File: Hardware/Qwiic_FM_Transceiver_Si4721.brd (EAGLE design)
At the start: 54.6 x 34.3 mm, 60 parts, among them J1 AUDIO_JACK_3.5MM_SMD, J2 AUDIO_JACK_3.5MM_SMD, J4 QWIIC_RIGHT_ANGLE, J5 QWIIC_RIGHT_ANGLE, U1 SI4721, U3 TPA6111A2DR, Y1 32.768kHz

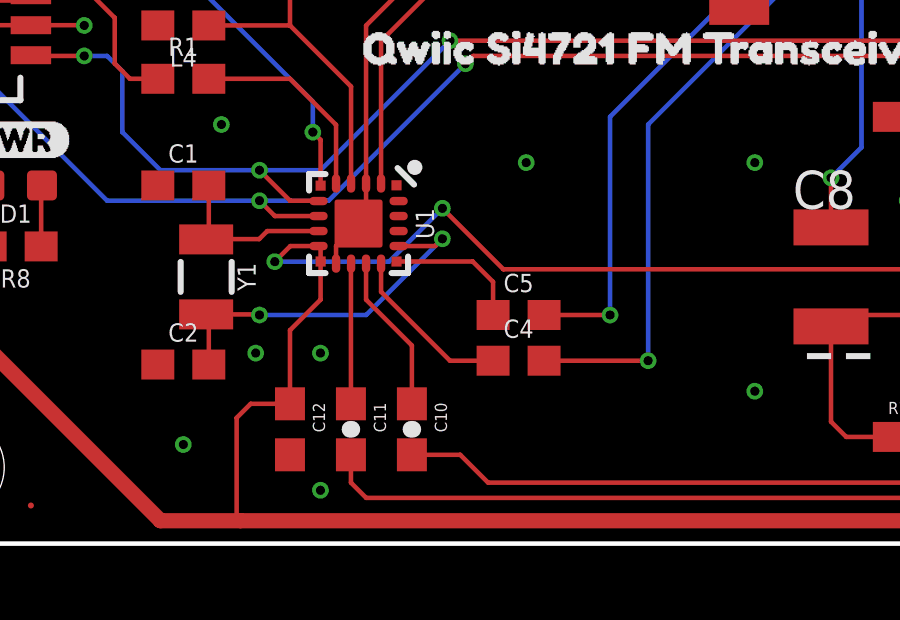
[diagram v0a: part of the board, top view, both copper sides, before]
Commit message: x01 protos ordered
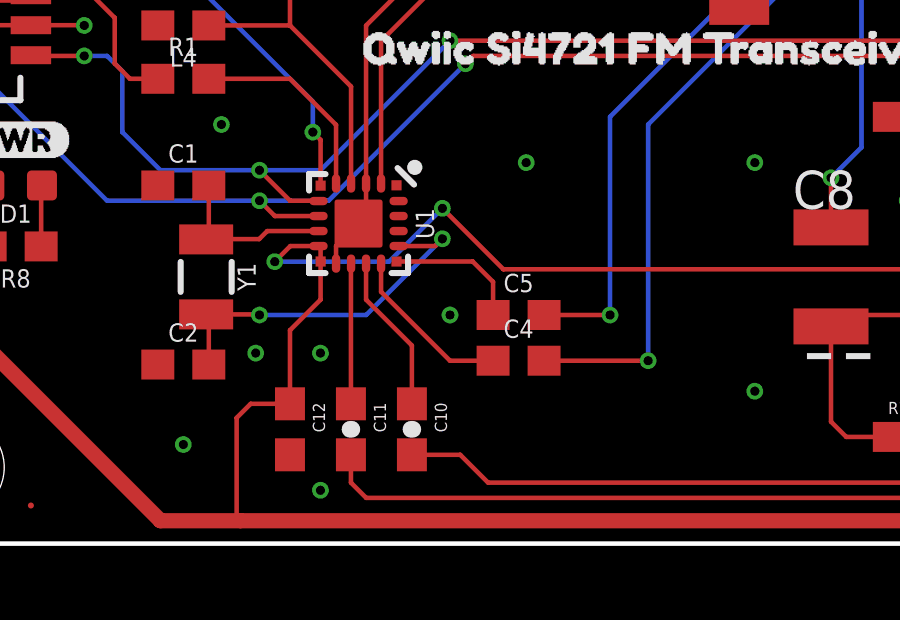
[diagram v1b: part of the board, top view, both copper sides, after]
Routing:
- net GND: vias 17 -> 18
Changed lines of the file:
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@@
 <layer number="23" name="tOrigins" color="15" fill="1" visible="yes" active="yes"/>
 <layer number="24" name="bOrigins" color="15" fill="1" visible="yes" active="yes"/>
-<layer number="25" name="tNames" color="7" fill="1" visible="no" active="yes"/>
-<layer number="26" name="bNames" color="7" fill="1" visible="no" active="yes"/>
-<layer number="27" name="tValues" color="7" fill="1" visible="no" active="yes"/>
-<layer number="28" name="bValues" color="7" fill="1" visible="no" active="yes"/>
-<layer number="29" name="tStop" color="7" fill="3" visible="no" active="yes"/>
-<layer number="30" name="bStop" color="7" fill="6" visible="no" active="yes"/>
-<layer number="31" name="tCream" color="7" fill="4" visible="no" active="yes"/>
-<layer number="32" name="bCream" color="7" fill="5" visible="no" active="yes"/>
-<layer number="33" name="tFinish" color="6" fill="3" visible="no" active="yes"/>
-<layer number="34" name="bFinish" color="6" fill="6" visible="no" active="yes"/>
-<layer number="35" name="tGlue" color="7" fill="4" visible="no" active="yes"/>
-<layer number="36" name="bGlue" color="7" fill="5" visible="no" active="yes"/>
-<layer number="37" name="tTest" color="7" fill="1" visible="no" active="yes"/>
-<layer number="38" name="bTest" color="7" fill="1" visible="no" active="yes"/>
-<layer number="39" name="tKeepout" color="4" fill="11" visible="no" active="yes"/>
-<layer number="40" name="bKeepout" color="1" fill="11" visible="no" active="yes"/>
-<layer number="41" name="tRestrict" color="4" fill="10" visible="no" active="yes"/>
-<layer number="42" name="bRestrict" color="1" fill="10" visible="no" active="yes"/>
-<layer number="43" name="vRestrict" color="2" fill="10" visible="no" active="yes"/>
-<layer number="44" name="Drills" color="7" fill="1" visible="no" active="yes"/>
+<layer number="25" name="tNames" color="7" fill="1" visible="yes" active="yes"/>
+<layer number="26" name="bNames" color="7" fill="1" visible="yes" active="yes"/>
+<layer number="27" name="tValues" color="7" fill="1" visible="yes" active="yes"/>
+<layer number="28" name="bValues" color="7" fill="1" visible="yes" active="yes"/>
+<layer number="29" name="tStop" color="7" fill="3" visible="yes" active="yes"/>
+<layer number="30" name="bStop" color="7" fill="6" visible="yes" active="yes"/>
+<layer number="31" name="tCream" color="7" fill="4" visible="yes" active="yes"/>
+<layer number="32" name="bCream" color="7" fill="5" visible="yes" active="yes"/>
+<layer number="33" name="tFinish" color="6" fill="3" visible="yes" active="yes"/>
+<layer number="34" name="bFinish" color="6" fill="6" visible="yes" active="yes"/>
+<layer number="35" name="tGlue" color="7" fill="4" visible="yes" active="yes"/>
+<layer number="36" name="bGlue" color="7" fill="5" visible="yes" active="yes"/>
+<layer number="37" name="tTest" color="7" fill="1" visible="yes" active="yes"/>
+<layer number="38" name="bTest" color="7" fill="1" visible="yes" active="yes"/>
+<layer number="39" name="tKeepout" color="4" fill="11" visible="yes" active="yes"/>
+<layer number="40" name="bKeepout" color="1" fill="11" visible="yes" active="yes"/>
+<layer number="41" name="tRestrict" color="4" fill="10" visible="yes" active="yes"/>
+<layer number="42" name="bRestrict" color="1" fill="10" visible="yes" active="yes"/>
+<layer number="43" name="vRestrict" color="2" fill="10" visible="yes" active="yes"/>
+<layer number="44" name="Drills" color="7" fill="1" visible="yes" active="yes"/>
 <layer number="45" name="Holes" color="7" fill="1" visible="yes" active="yes"/>
 <layer number="46" name="Milling" color="3" fill="1" visible="yes" active="yes"/>
-<layer number="47" name="Measures" color="7" fill="1" visible="no" active="yes"/>
-<layer number="48" name="Document" color="7" fill="1" visible="no" active="yes"/>
-<layer number="49" name="Reference" color="7" fill="1" visible="no" active="yes"/>
-<layer number="50" name="dxf" color="7" fill="1" visible="no" active="yes"/>
+<layer number="47" name="Measures" color="7" fill="1" visible="yes" active="yes"/>
+<layer number="48" name="Document" color="7" fill="1" visible="yes" active="yes"/>
+<layer number="49" name="Reference" color="7" fill="1" visible="yes" active="yes"/>
+<layer number="50" name="dxf" color="7" fill="1" visible="yes" active="yes"/>
 <layer number="51" name="tDocu" color="6" fill="1" visible="yes" active="yes"/>
-<layer number="52" name="bDocu" color="7" fill="1" visible="no" active="yes"/>
+<layer number="52" name="bDocu" color="7" fill="1" visible="yes" active="yes"/>
 <layer number="91" name="Nets" color="2" fill="1" visible="no" active="no"/>
 <layer number="92" name="Busses" color="1" fill="1" visible="no" active="no"/>
@@
 <via x="21.59" y="29.21" extent="1-16" drill="0.3048"/>
 <via x="36.83" y="29.21" extent="1-16" drill="0.3048"/>
+<via x="19.05" y="7.62" extent="1-16" drill="0.3048"/>
 </signal>
 <signal name="LIN">

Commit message: x02 hardware order
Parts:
- added C13: 2.2uF, SparkFun-Capacitors:0603
- added U$17: (no value), addr_labels:OPEN_0X631
- U$15: device defaultadr:DEFAULT#_0X110 -> addr_labels:CLOSED_0X110
- moved L4 1.78 mm to (10.2, 19.1)
- moved U$15 0.76 mm to (1.91, 29.8)
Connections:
- net GND: now also C13.2
- net N$1: now also C13.1
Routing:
- net N$1: track 6.83 -> 8.61 mm
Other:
- board text added: "What Size Antenna Should You Use? ------------------------- ½ wave FM whip antenna ≌ 160cm ¼ wave FM whip antenna ≌ 80cm (practically, for desktop testing purposes, jamming any piece of wire in there will work)"
- board text added: "x02"
- board text removed: "x01"
